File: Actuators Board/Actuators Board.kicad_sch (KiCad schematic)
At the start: 71 parts, among them IC1 BD62120AEFJ-E2, J1 Conn_01x05_Male, J10 Conn_01x02_Male, J2 Solenoid(Sol), J4 Conn_01x03_Male, J5 Conn_01x06_Male, J9 Conn_01x02_Male, Q1 MMDT2222A, Q2 SI2366DS, U1 ESP32-PICO-D4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

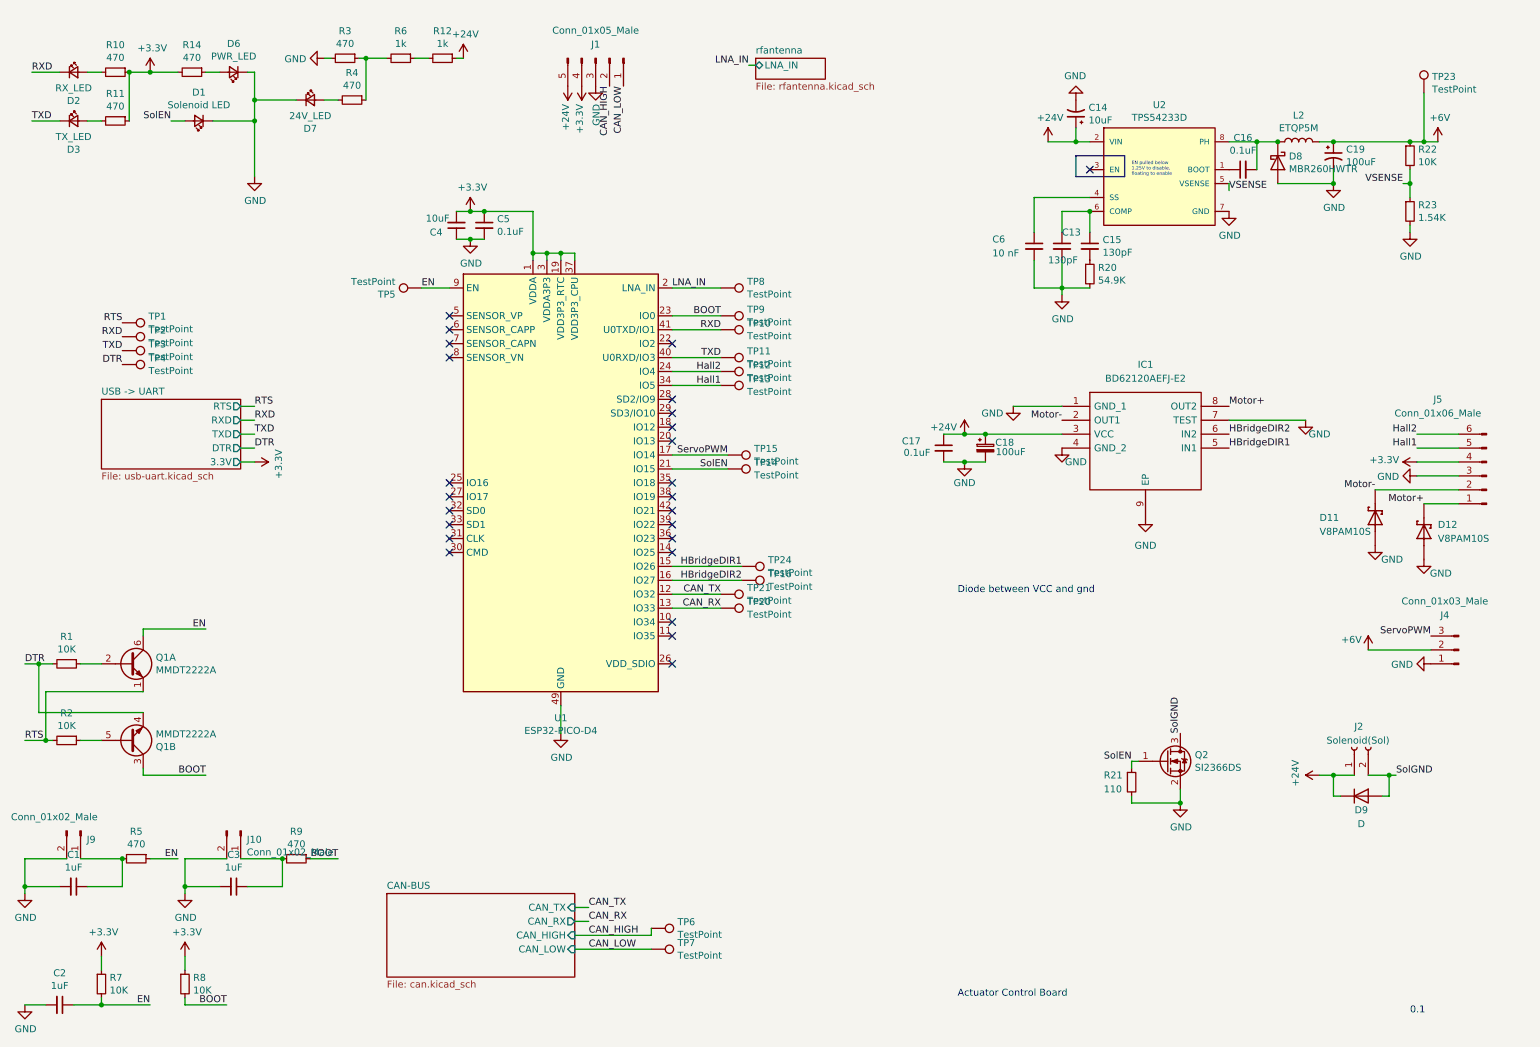
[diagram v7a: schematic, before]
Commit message: Reconfigured uart converter to disable 5->3.3V regulation
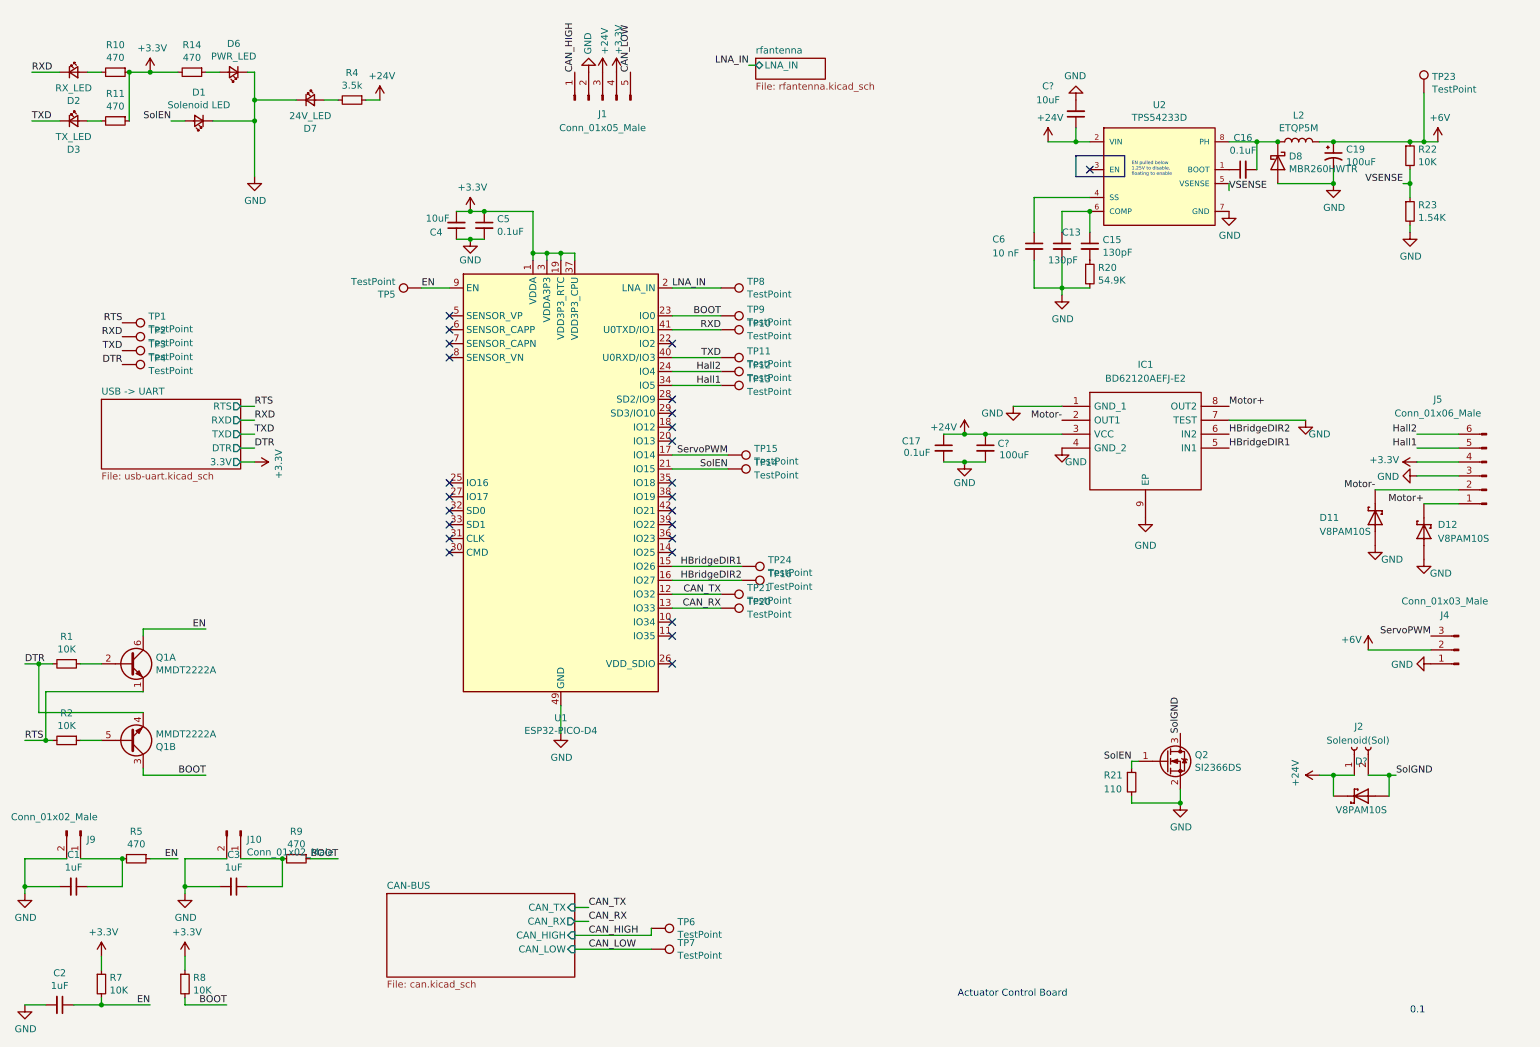
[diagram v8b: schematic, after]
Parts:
- removed C14: 10uF, Capacitor_SMD:CP_Elec_3x5.3, symbol Device:CP1_Small
- removed C18: 100uF, Capacitor_SMD:CP_Elec_5x5.9, symbol Device:C_Polarized_Small
- removed D9: D, Diode_SMD:D_0603_1608Metric, symbol Device:D
- removed R12, R6: 1k, Resistor_SMD:R_0603_1608Metric, symbol Device:R_Small
- removed R3: 470, Resistor_SMD:R_0603_1608Metric, symbol Device:R_Small
- added C?: 100uF, Capacitor_SMD:C_0603_1608Metric, symbol Device:C_Small
- added C?: 10uF, Capacitor_SMD:C_0603_1608Metric, symbol Device:C_Small
- added D?: V8PAM10S, iclr:DIO_V3PAN50-M3_I, symbol iclr:V3PAN50-M3{brace}slash}I
- R4: value 470 -> 3.5k
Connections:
- net +24V: now also J1.3 (Pin_3), R4.1, C?.1, C?.1, D?.C; no longer J1.5 (Pin_5)
- net CAN_HIGH: now also J1.1 (Pin_1); no longer J1.2 (Pin_2)
- net CAN_LOW: now also J1.5 (Pin_5); no longer J1.1 (Pin_1)
- net GND: now also J1.2 (Pin_2), C?.2, C?.2; no longer J1.3 (Pin_3)
- net SolGND: now also D?.A
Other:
- note removed: "Diode between VCC and gnd"
- moved on the sheet: J1
